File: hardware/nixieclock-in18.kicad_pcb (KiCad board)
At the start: 2 copper layers, 151.1 x 47 mm, 84 parts, among them J1 PROG, J2 POWER, Q1 BC848, Q10 MMBTA42, Q11 MMBTA42, Q12 MMBTA42, Q13 MMBTA42, Q14 MMBTA42, Q15 MMBTA42, Q16 MMBTA42, Q17 MMBTA42, Q18 MMBTA42, Q19 MMBTA42, Q2 BC858, Q20 MMBTA42, Q21 MMBTA42, Q3 Si4434, Q4 MMBTA42, Q5 MMBTA42, Q6 MMBTA42, Q7 MMBTA42, Q8 MMBTA42, Q9 MMBTA42, T1 IN18, T2 IN18, T3 IN18, T4 IN18, U1 LM1117-3.3, U2 DS3231M, U3 LM393, U4 ESP32-WROOM-32D

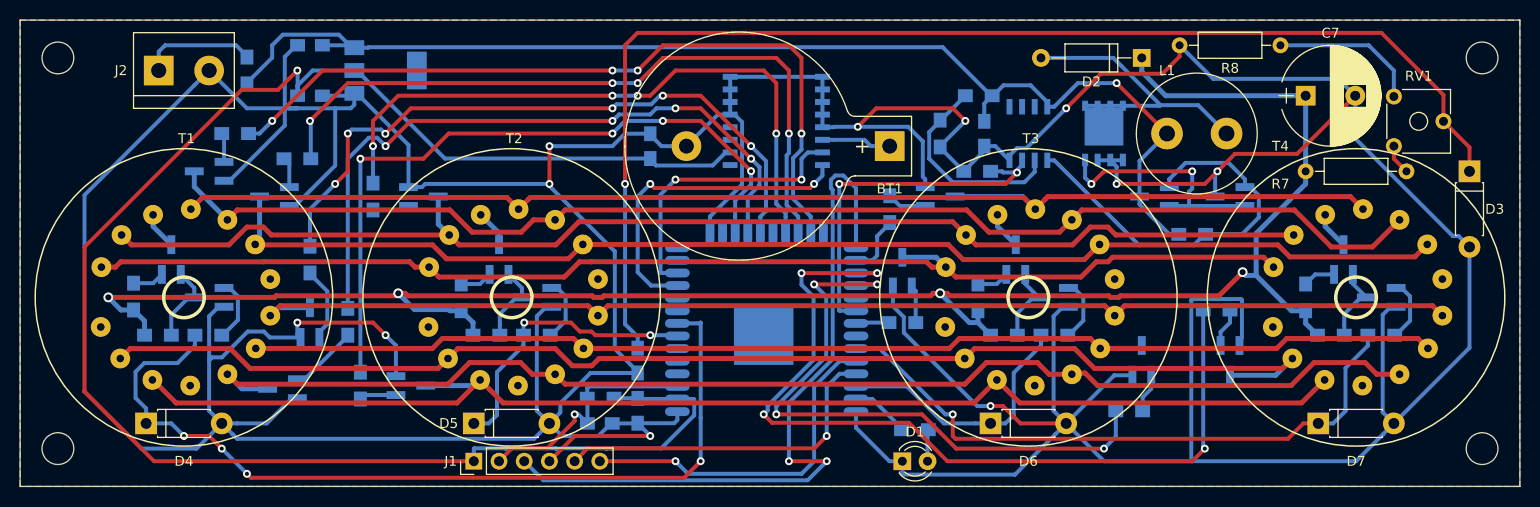
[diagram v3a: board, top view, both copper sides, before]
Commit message: change DIG5 pin (programmin flash issue)
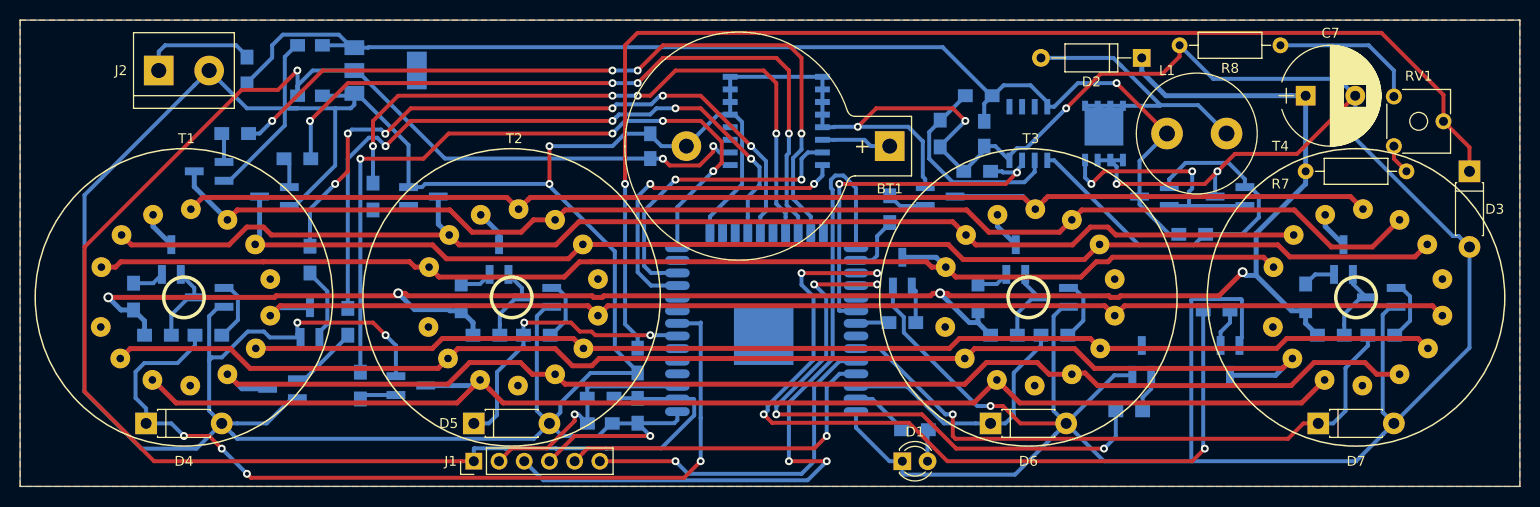
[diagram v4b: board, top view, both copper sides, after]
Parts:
- removed REF** (x4): MountingHole_3.2mm_M3, Mounting_Holes:MountingHole_3.2mm_M3
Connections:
- U4 pad 14: (no net) -> DIG5
- U4 pad 17: DIG5 -> (no net)
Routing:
- net I2C_SDA: track 28.9 -> 30.8 mm
- net DIG5: track 71.4 -> 72.9 mm
- net +3V3: track 172.6 -> 173.9 mm, vias 1 -> 3
